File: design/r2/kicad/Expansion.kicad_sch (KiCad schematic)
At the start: 31 parts, among them IC1 MC68010P10, IC7 74LS148, J3 Conn_02x32_Odd_Even, J5 PWR, J6 Conn_01x05_Male, J8 Conn_01x02_Male, J9 Jack-DC

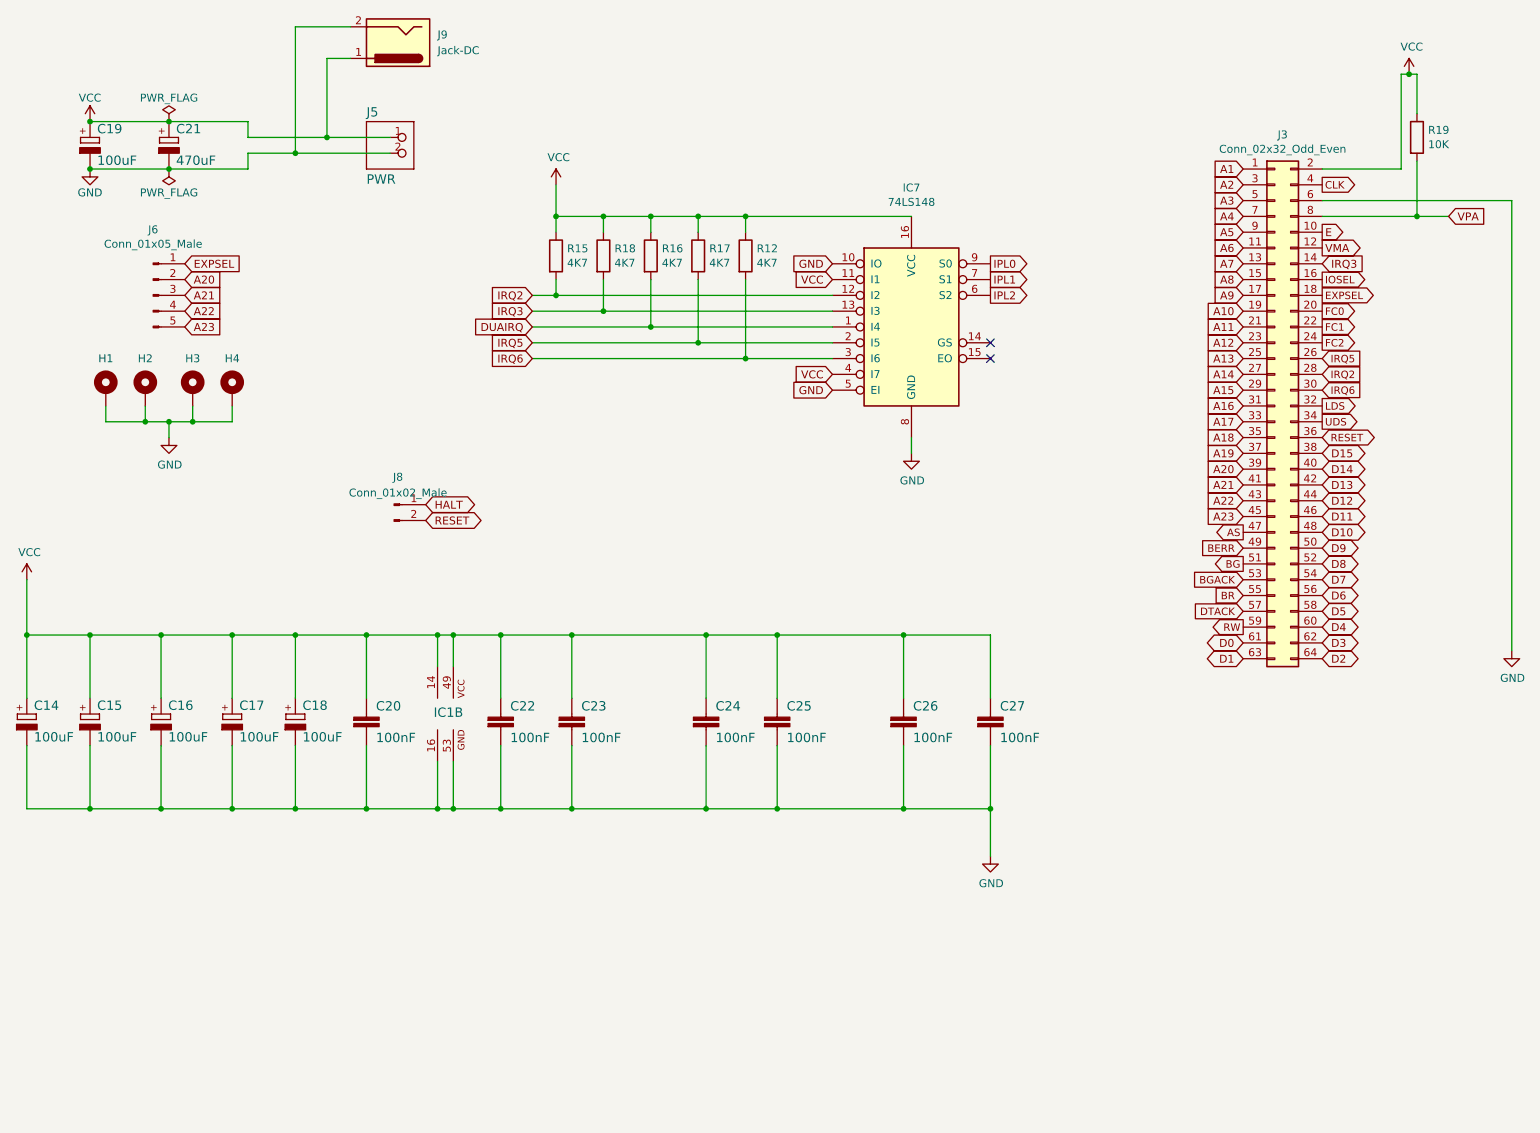
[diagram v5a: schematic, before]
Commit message: Tentative r2 SMD design
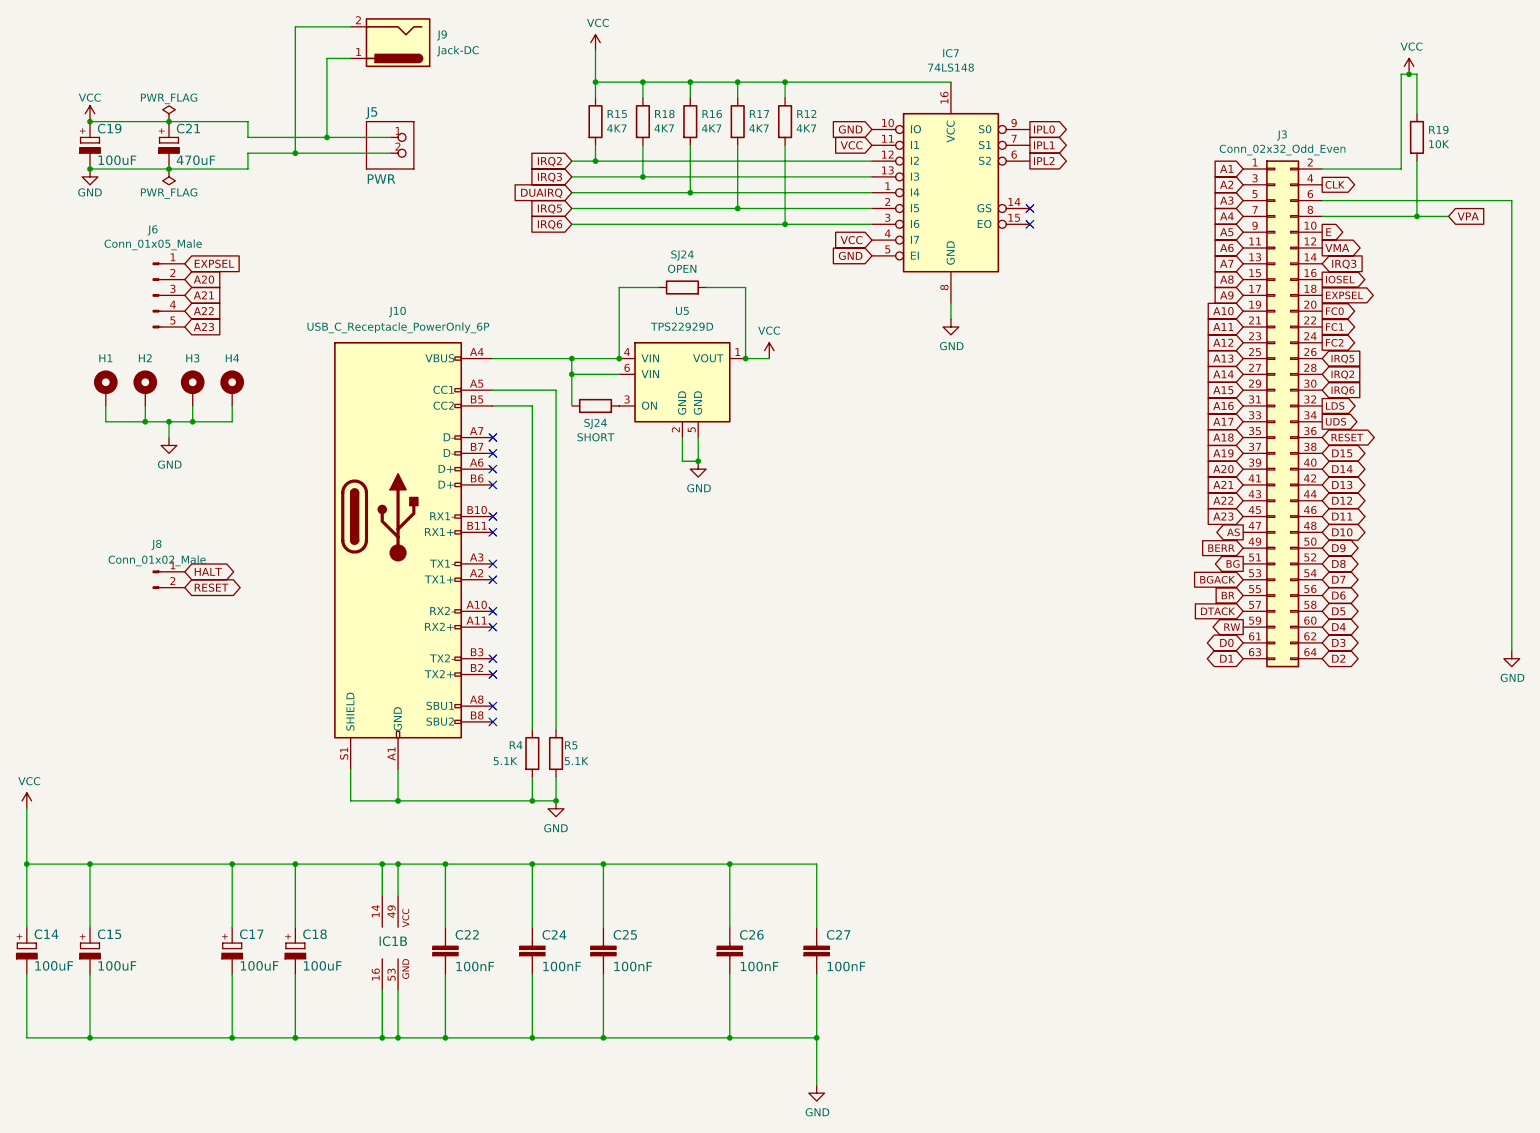
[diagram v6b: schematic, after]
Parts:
- removed C16: 100uF, rosco_m68k:E2,5-5, symbol rosco_m68k-eagle-import:CPOL-EUE2.5-5
- removed C20, C23: 100nF, rosco_m68k:C2.5-3, symbol rosco_m68k-eagle-import:C2,5-3
- added J10: USB_C_Receptacle_PowerOnly_6P, Connector_USB:USB_C_Receptacle_Palconn_UTC16-G, symbol Connector:USB_C_Receptacle
- added R4, R5: 5.1K, Resistor_SMD:R_0201_0603Metric, symbol Device:R
- added SJ24: OPEN, Jumper:SolderJumper-2_P1.3mm_Open_RoundedPad1.0x1.5mm, symbol Device:R
- added SJ24: SHORT, Jumper:SolderJumper-2_P1.3mm_Bridged_RoundedPad1.0x1.5mm, symbol Device:R
- added U5: TPS22929D, Package_TO_SOT_SMD:SOT-23-6, symbol Power_Management:TPS22929D
- C22, C24, C25, C26, C27: footprint rosco_m68k:C2.5-3 -> Capacitor_SMD:C_0603_1608Metric
- R12, R15, R16, R17, R18, R19: footprint rosco_m68k:0207_10 -> Resistor_SMD:R_0603_1608Metric
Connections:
- net GND: now also J10.A1 (GND), J10.A12 (GND), J10.B1 (GND), J10.B12 (GND), J10.S1 (SHIELD), R4.2, R5.1, U5.2 (GND), U5.5 (GND)
- net VCC: now also SJ24.2, U5.1 (VOUT)
- new net: J10.A4 (VBUS), J10.A9 (VBUS), J10.B4 (VBUS), J10.B9 (VBUS), SJ24.1, SJ24.1, U5.4 (VIN), U5.6 (VIN)
- new net: SJ24.2, U5.3 (ON)
- new net: J10.B5 (CC2), R4.1
- new net: J10.A5 (CC1), R5.2
- no-connect marks 2 -> 16
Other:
- moved on the sheet: C14, C15, C17, C18, C22, C24, C25, C26, C27, IC1B, IC7, J8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

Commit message: Resize tiny resistors
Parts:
- R4, R5: footprint Resistor_SMD:R_0201_0603Metric -> Resistor_SMD:R_0603_1608Metric
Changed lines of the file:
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@@
       (effects (font (size 1.27 1.27)) (justify left))
     )
-    (property "Footprint" "Resistor_SMD:R_0201_0603Metric" (at 98.552 137.16 90)
+    (property "Footprint" "Resistor_SMD:R_0603_1608Metric" (at 98.552 137.16 90)
       (effects (font (size 1.27 1.27)) hide)
     )
@@
       (effects (font (size 1.27 1.27)) (justify right))
     )
-    (property "Footprint" "Resistor_SMD:R_0201_0603Metric" (at 105.918 137.16 90)
+    (property "Footprint" "Resistor_SMD:R_0603_1608Metric" (at 105.918 137.16 90)
       (effects (font (size 1.27 1.27)) hide)
     )

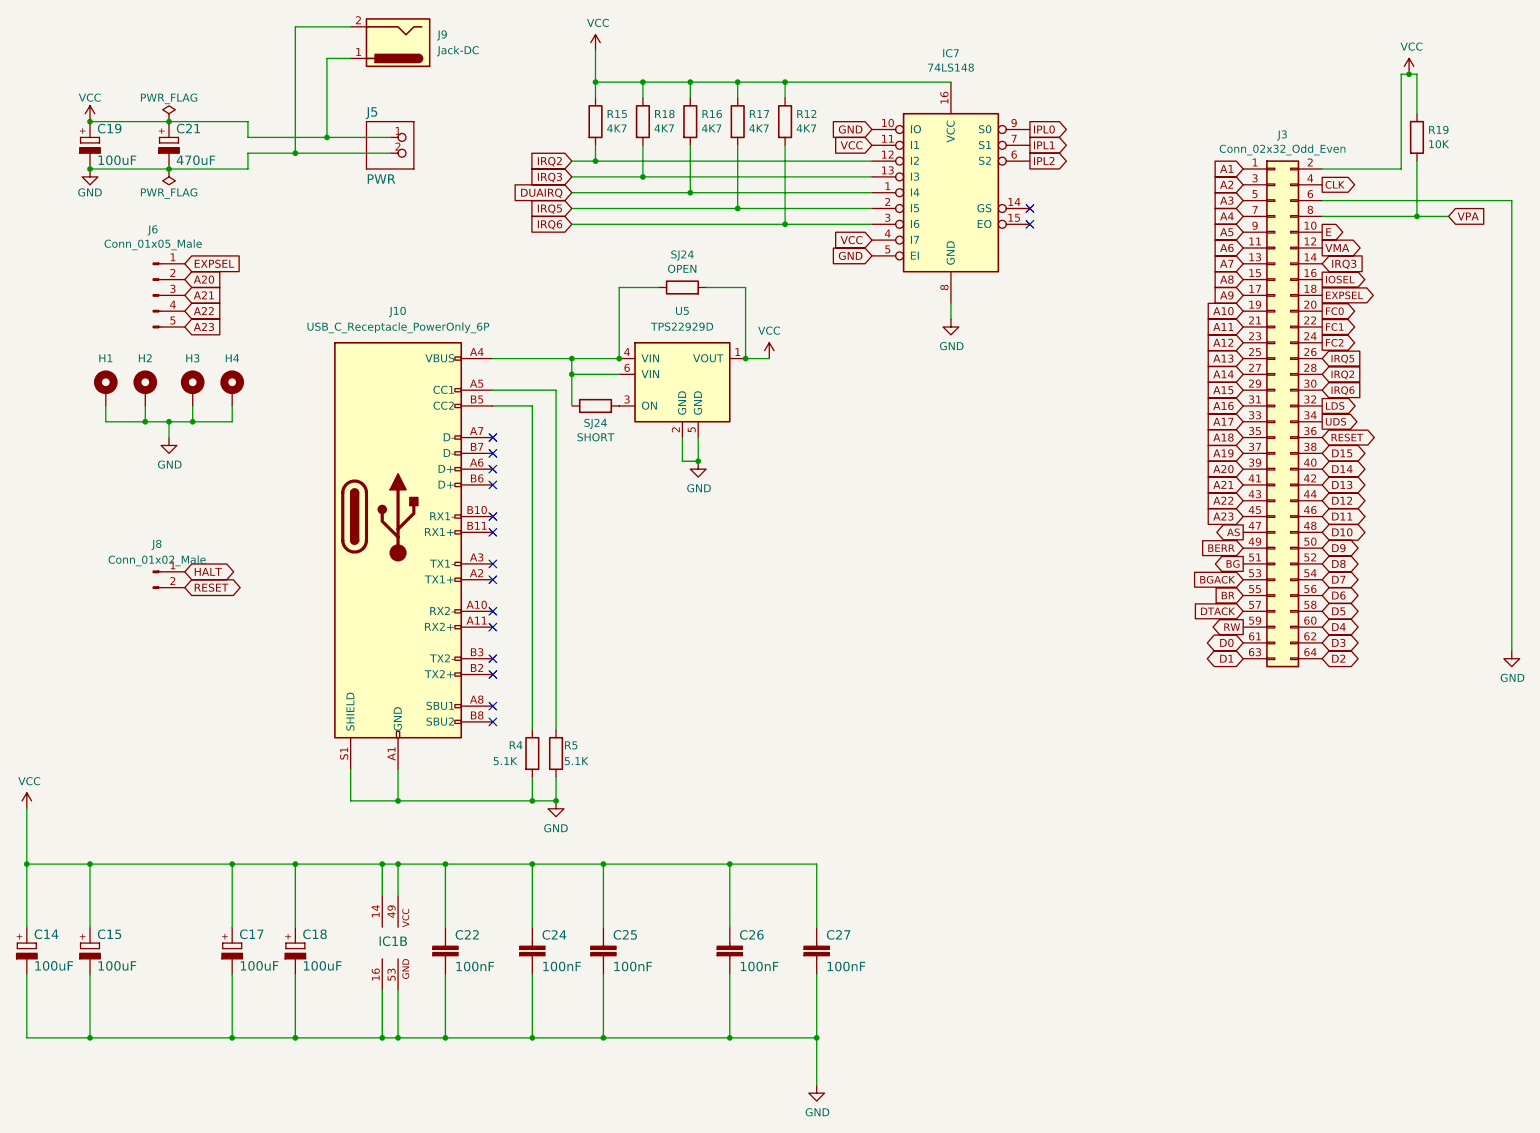
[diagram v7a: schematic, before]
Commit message: Reroute for FTDI
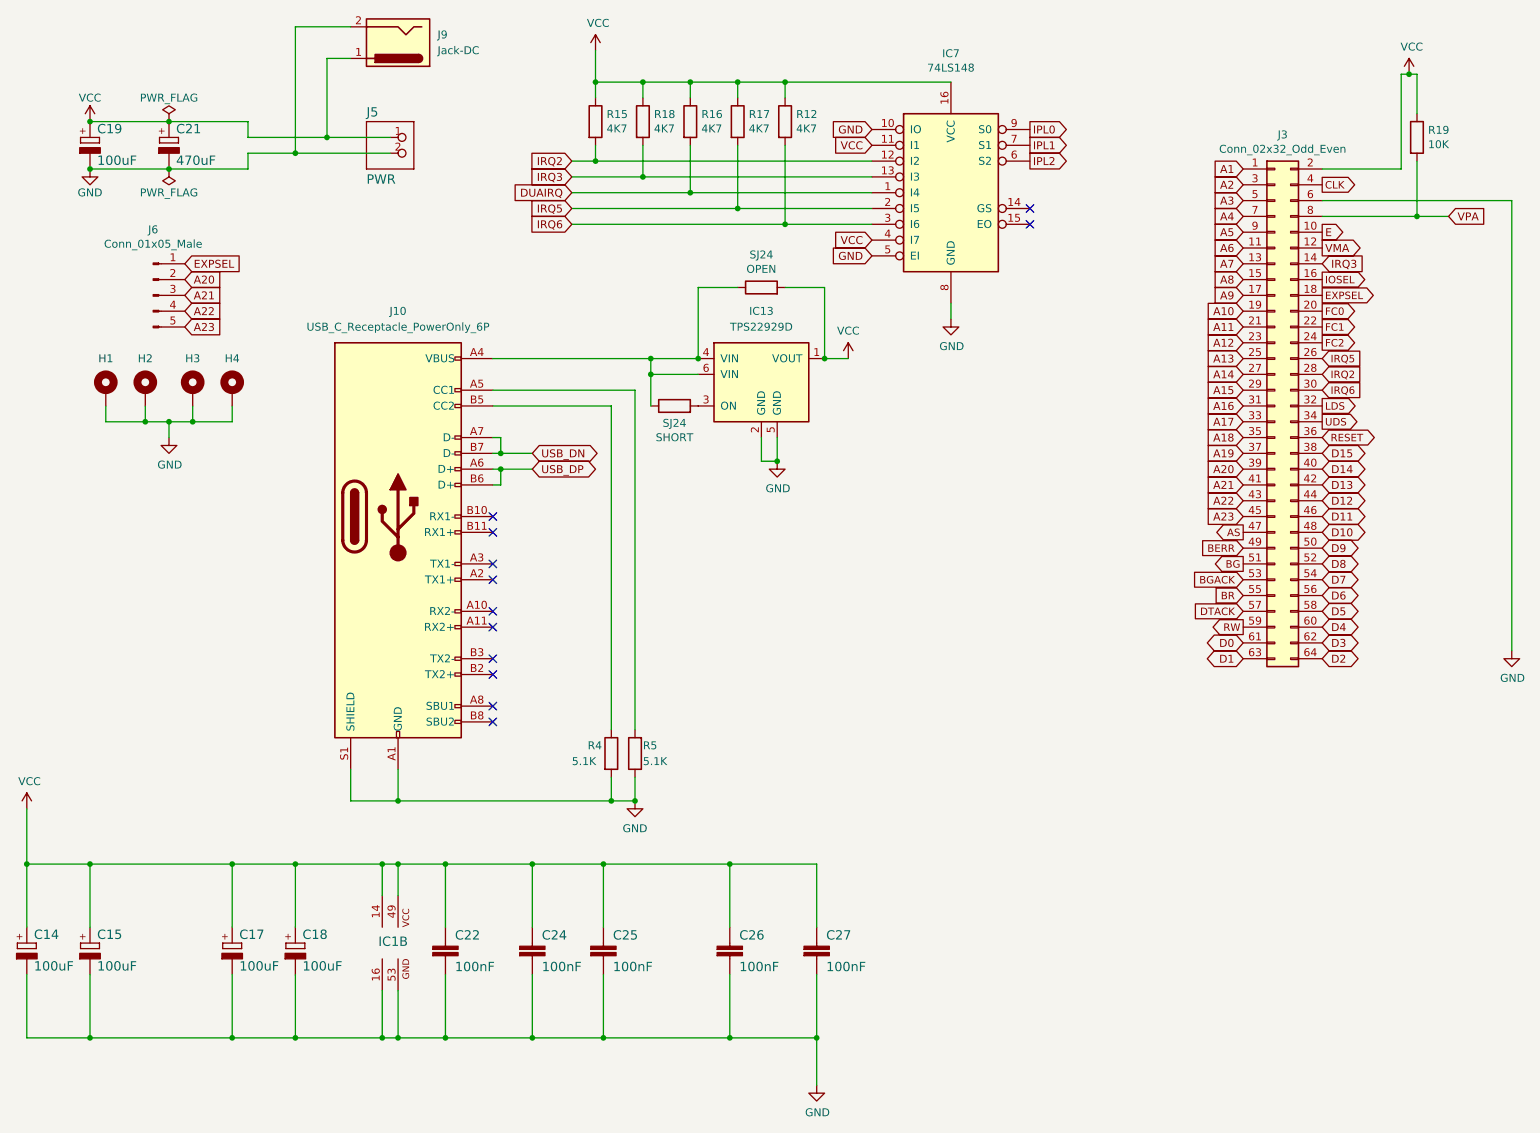
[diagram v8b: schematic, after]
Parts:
- removed J8: Conn_01x02_Male, Connector_PinHeader_2.54mm:PinHeader_1x02_P2.54mm_Vertical, symbol Connector:Conn_01x02_Pin
- renumbered U5 to IC13
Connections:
- net USB_DP: now reaches J10.A6 (D+)
- net USB_DP: now also J10.B6 (D+)
- net USB_DN: now reaches J10.A7 (D-)
- net USB_DN: now also J10.B7 (D-)
- no-connect marks 16 -> 12
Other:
- moved on the sheet: IC13, R4, R5, SJ24
